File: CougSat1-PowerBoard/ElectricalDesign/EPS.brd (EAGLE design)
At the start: 91.4 x 95.8 mm, 255 parts, among them J1 PV0, J2 PV1, J3 PV2, J4 PV3, J5 Umbilical, J6 SWD, J7 CougSat Card, J8 Deployables, Q1 NTLUD3A50PZ, Q10 DMN2008LFU, Q11 DMN2008LFU, Q12 CSD25402Q3A, Q13 CSD25402Q3A, Q14 NTLUD3A50PZ, Q15 NTLUD3A50PZ, Q16 NTLUD3A50PZ, Q17 NTLUD3A50PZ, Q18 NTLUD3A50PZ, Q19 NTLUD3A50PZ, Q2 NTLUD3A50PZ, Q20 NTLUD3A50PZ, Q21 NTLUD3A50PZ, Q22 NTLUD3A50PZ, Q23 CSD25402Q3A, Q24 CSD25402Q3A, Q25 DMN53D0L, Q26 NTLUD3A50PZ, Q27 NTLUD3A50PZ, Q28 NTLUD3A50PZ, Q29 NTLUD3A50PZ, Q3 NTLUD3A50PZ, Q30 NTLUD3A50PZ, Q31 NTLUD3A50PZ, Q32 NTLUD3A50PZ, Q33 NTLUD3A50PZ, Q34 NTLUD3A50PZ, Q35 NTLUD3A50PZ, Q36 NTLUD3A50PZ, Q37 NTLUD3A50PZ, Q38 NTLUD3A50PZ, Q39 NTLUD3A50PZ, Q4 NTLUD3A50PZ, Q40 NTLUD3A50PZ, Q41 NTLUD3A50PZ, Q42 NTLUD3A50PZ, Q43 NTLUD3A50PZ, Q5 NTLUD3A50PZ, Q6 NTLUD3A50PZ, Q7 NTLUD3A50PZ, Q8 NTLUD3A50PZ, Q9 NTLUD3A50PZ, SW1 D2MQ-1-TL, U1 BQ29700, U10 LTC2499, U11 LTC2499, U12 LTC2499, U13 LTC2499, U14 MCP1501-18, U15 LTC2499, U2 BQ29700, U3 TPS64200, U4 TPS64200, U5 STM32L476RGT, U6 TCA9535R, U7 SN74LVC244AR, U8 TCA9535R, U9 LTC2499

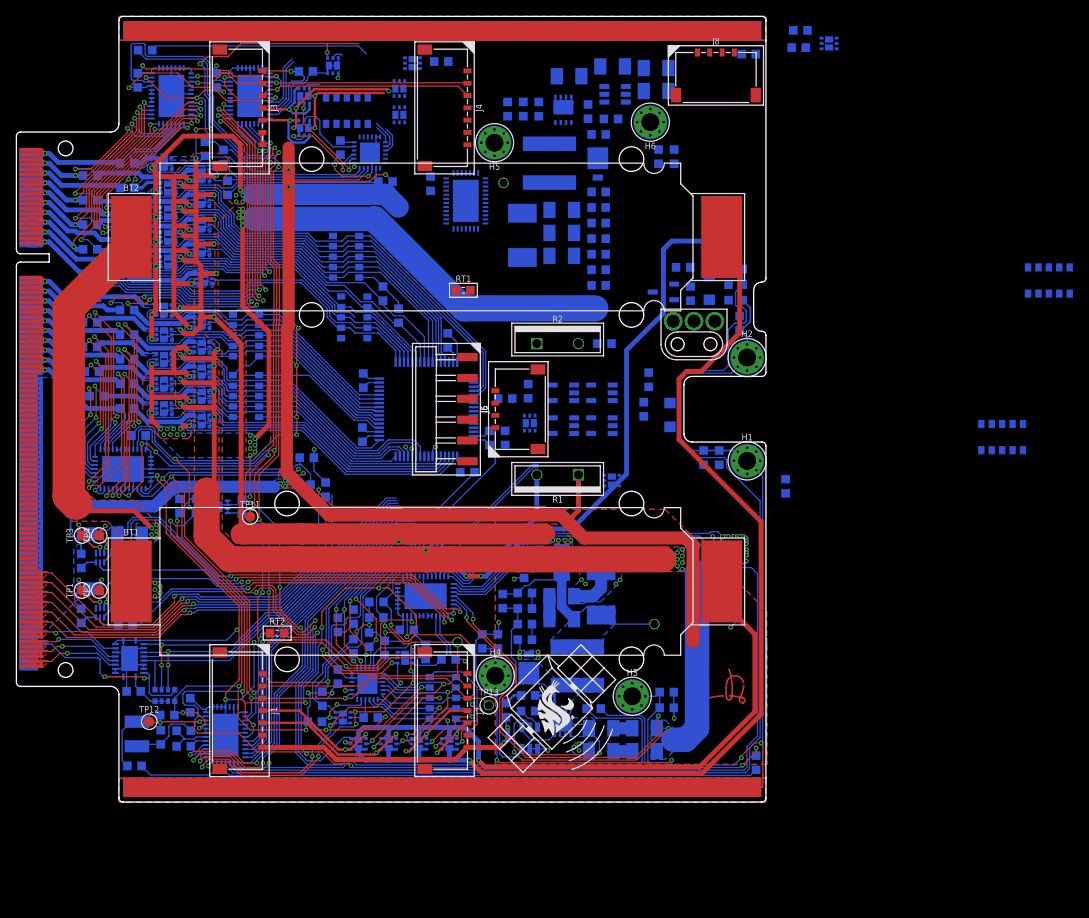
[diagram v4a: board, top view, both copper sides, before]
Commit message: Laid Out JTAG
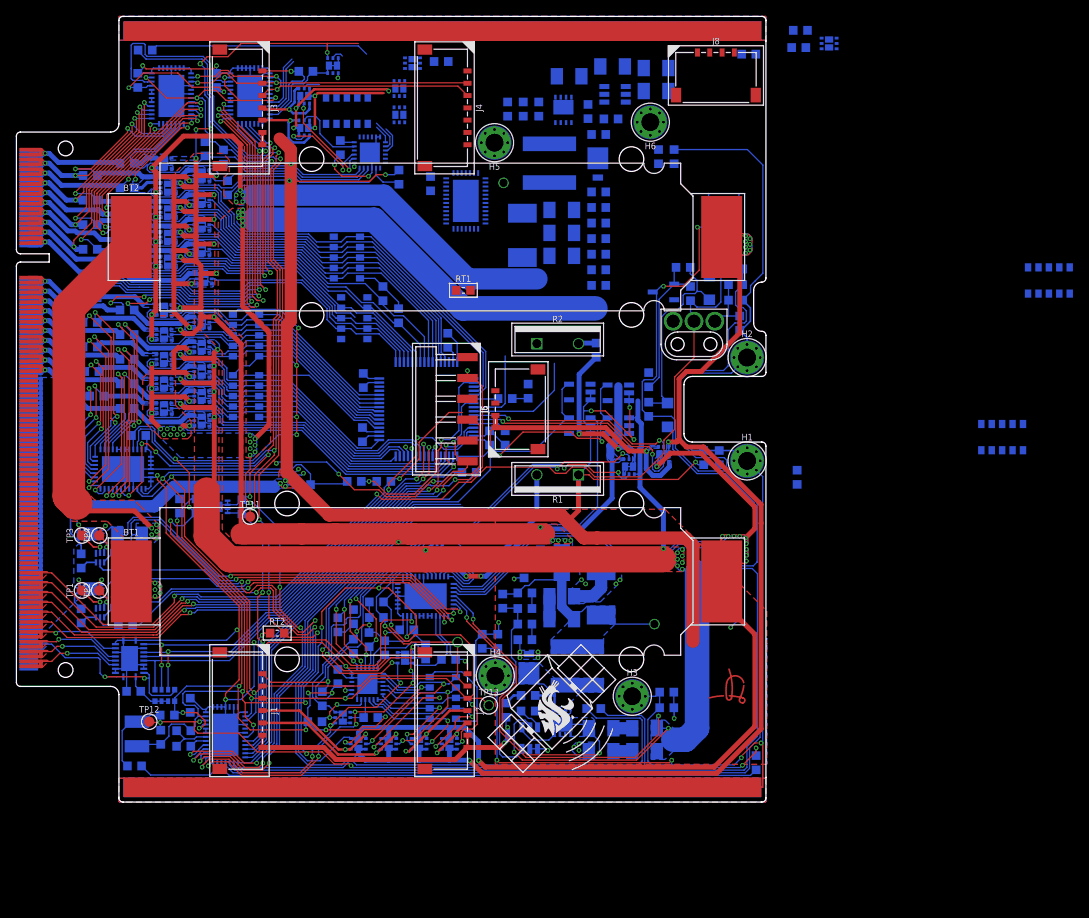
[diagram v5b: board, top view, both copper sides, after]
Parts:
- moved Q9 16.7 mm to (78.9, -5.50), turned to 270 degrees
- moved R78 7.17 mm to (44.8, -8.80), turned to 180 degrees
- moved C22 6.48 mm to (41.2, -8.80)
- moved Q43 2.70 mm to (74.7, -7.00), turned to 90 degrees
- moved D6 2.00 mm to (68.7, 2.10)
- moved D5 2.00 mm to (68.7, -2.00)
- moved D7 2.00 mm to (73.4, -2.00)
- moved D8 2.00 mm to (73.4, 2.00)
- moved R61 1.78 mm to (95.2, -8.30), turned to 270 degrees
- moved R83 1.74 mm to (46.6, 28.3), turned to 270 degrees
- moved R57 1.28 mm to (70.7, 7.20), turned to 270 degrees
- moved R11 0.60 mm to (77.1, 0.00), turned to 270 degrees
- moved D2 0.30 mm to (79.4, -0.70)
- moved RT6 0.20 mm to (55.2, -7.70)
- moved RN2 0.14 mm to (40.3, 18.5)
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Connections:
- net UMB_SW-A: now also U5.58; no longer U5.59
- net UMB_SW-B: now also U5.59; no longer U5.58
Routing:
- net !BATT_SW_CTRL: track 1.19 -> 66.2 mm, vias 1 -> 2
- net PGND: track 382.2 -> 437.4 mm, vias 24 -> 28
- net VIN-A: track 192.7 -> 238.0 mm, vias 14 -> 15
- net PWR_CTRL_SW: track 81.0 -> 122.9 mm
- net CHASSIS: track 224.0 -> 253.1 mm
- net UMB_IN: track 56.0 -> 85.0 mm, vias 1 -> 2
- net VBATT: track 0.00 -> 28.9 mm, vias 0 -> 2
- net UMB_SW-B: track 0.00 -> 27.9 mm, vias 0 -> 2
- net AVDD: track 212.2 -> 239.3 mm, vias 10 -> 13
- net JTAG_TCK: track 43.8 -> 70.3 mm, vias 2 -> 4
- net UMB_SW-A: track 0.00 -> 25.4 mm, vias 0 -> 2
- net BATT_SW_VIN: track 0.00 -> 24.9 mm
- net 3.3V-B: track 159.5 -> 183.8 mm
- net VBATT-A: track 325.1 -> 349.3 mm, vias 19 -> 20
- net I_BH-1: track 0.00 -> 21.8 mm, vias 0 -> 2
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- added copper zone on layer 16, net I_BH-1
- added copper zone on layer 16, net UMB_IN
- added copper zone on layer 1, net VIN-B
- added copper zone on layer 16, net VIN-B

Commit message: Laid Out Regulator B
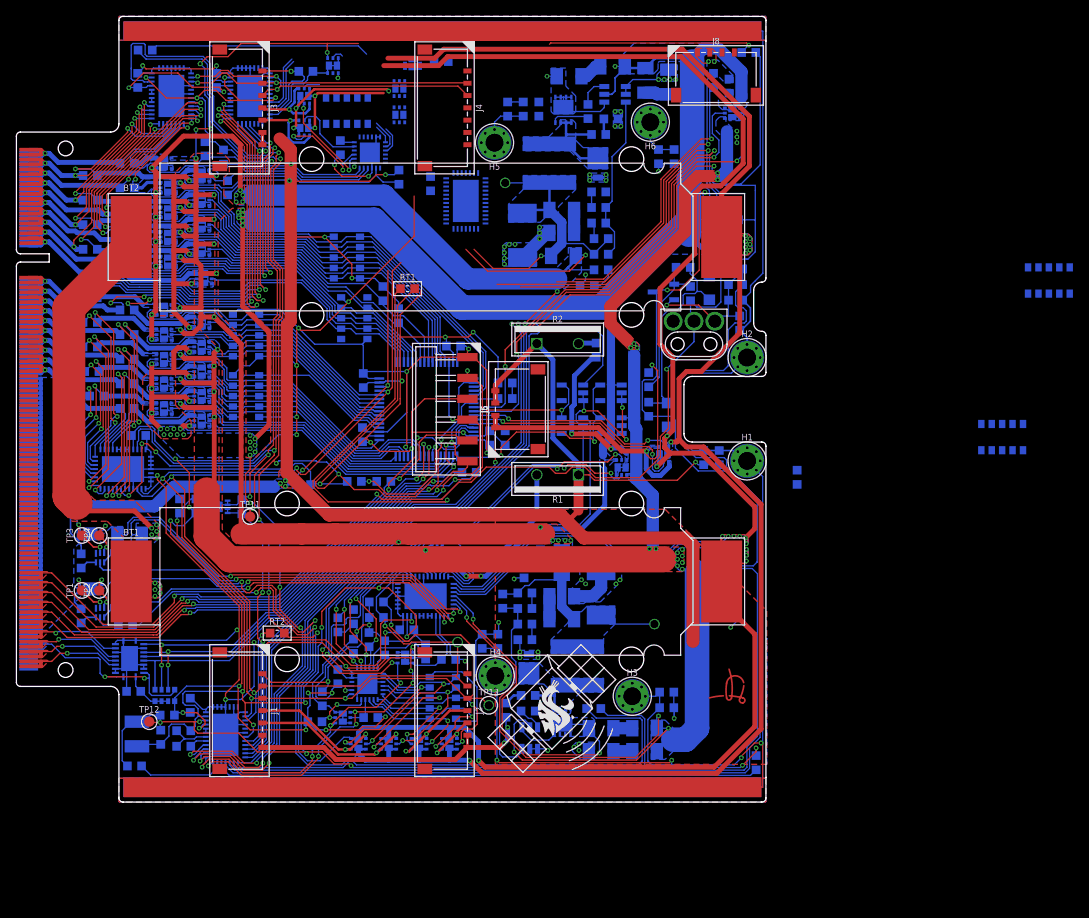
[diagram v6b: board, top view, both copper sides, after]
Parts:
- moved Q41 14.5 mm to (87.3, 36.1), turned to 180 degrees
- moved R55 11.1 mm to (85.0, 40.1), turned to 270 degrees
- moved R70 11.0 mm to (86.9, 39.4), turned to 270 degrees
- moved RT1 6.80 mm to (47.7, 14.7)
- moved R77 2.97 mm to (59.6, 3.20), turned to 180 degrees
- moved C5 1.98 mm to (76.7, 40.1), turned to 270 degrees
- moved C4 1.86 mm to (79.5, 39.9), turned to 90 degrees
- moved R75 1.40 mm to (69.6, 15.1), turned to 180 degrees
- moved DS2 1.00 mm to (85.4, 25.0), turned to 0 degrees
- moved C20 0.99 mm to (53.3, 7.70), turned to 0 degrees
- moved D6 0.91 mm to (67.8, 2.00)
- moved Q43 0.91 mm to (73.8, -7.10)
- moved D5 0.90 mm to (67.8, -2.00)
- moved D7 0.90 mm to (72.5, -2.00)
- moved D8 0.90 mm to (72.5, 2.00)
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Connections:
- net TEMP+X+Y: now also U13.21; no longer U13.12
- net TEMP-BATT-B: now also U13.11; no longer U13.21
- net UMB_IN: now also U13.12; no longer U13.11
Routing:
- net VBATT-B: track 204.3 -> 326.5 mm, vias 35 -> 37
- net VIN-B: track 222.8 -> 330.4 mm, vias 14 -> 15
- net PGND: track 437.4 -> 540.8 mm, vias 28 -> 57
- net TEMP+X+Y: track 45.6 -> 136.8 mm, vias 0 -> 4
- net 3.3V: track 243.0 -> 325.5 mm, vias 20 -> 25
- net 3.3V-B: track 183.8 -> 263.7 mm, vias 25 -> 28
- net DGND: track 254.7 -> 332.9 mm, vias 11 -> 17
- net VIN-A: track 238.0 -> 313.8 mm, vias 15 -> 16
- net AVDD: track 239.3 -> 297.9 mm, vias 13 -> 14
- net CHASSIS: track 253.1 -> 307.3 mm
- net PC_DEPLOY-A: track 9.84 -> 56.1 mm, vias 0 -> 2
- net PC_DEPLOY-B: track 14.2 -> 59.1 mm, vias 0 -> 2
- net VBATT-A: track 349.3 -> 391.7 mm, vias 20 -> 26
- net PR_DEPLOY: track 0.00 -> 37.5 mm, vias 0 -> 3
- net 3.3V_I-B: track 0.00 -> 37.1 mm, vias 0 -> 1
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- added copper zone on layer 16, net 3.3V_I-B
- added copper zone on layer 16, net 3.3V_ISENS-B
- added copper zone on layer 16, net 3.3V_REG_BUCK_NODE-B
- added copper zone on layer 16, net I_DEPLOY
- added copper zone on layer 1, net PR_DEPLOY
- added copper zone on layer 16, net PR_DEPLOY

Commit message: Laid Out Rest of Traces
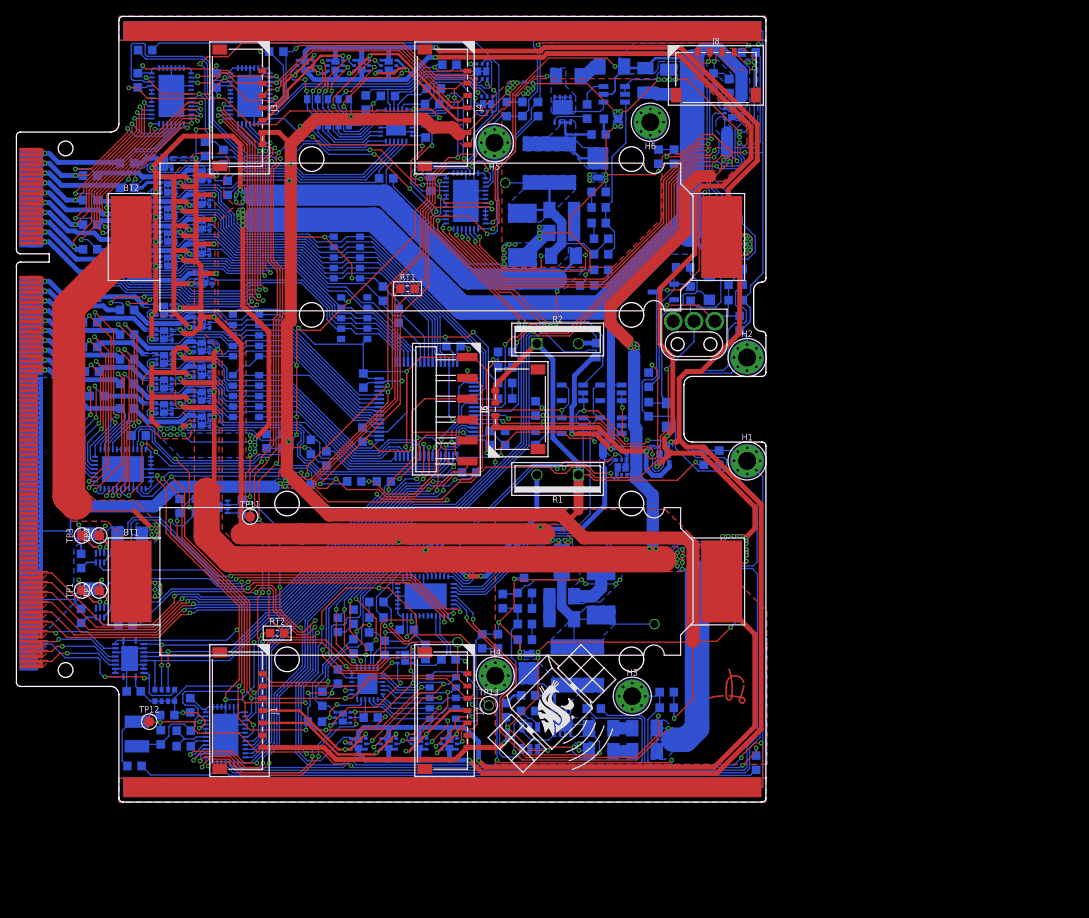
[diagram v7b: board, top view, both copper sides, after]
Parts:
- removed R61: 0Ω <20mΩ, CougsInSpace-Resistors:1608
- removed RN3, RN7: 10kΩ 5%, CougsInSpace-Resistors:3264
- added R100, R101, R102, R103, R104, R105, R94, R95, R96, R97, R98, R99: 10kΩ 0.1%, CougsInSpace-Resistors:1608
- moved Q32 19.4 mm to (57.4, 37.2)
- moved C24 10.6 mm to (49.9, 34.0)
- moved Q33 8.56 mm to (56.8, 41.2), turned to 270 degrees
- moved Q6 8.50 mm to (38.9, 41.9), turned to 180 degrees
- moved Q8 6.14 mm to (45.4, 41.9), turned to 180 degrees
- moved Q7 5.39 mm to (42.1, 41.9), turned to 180 degrees
- moved U6 4.60 mm to (46.3, 34.6), turned to 90 degrees
- moved R46 4.33 mm to (31.7, 43.6)
- moved Q5 3.70 mm to (35.2, 41.9), turned to 180 degrees
- moved RN1 2.31 mm to (38.0, 36.2)
- moved R83 1.56 mm to (45.1, 28.1), turned to 0 degrees
- moved R47 1.08 mm to (52.8, 42.0), turned to 180 degrees
- moved Q12 0.10 mm to (66.6, 36.5)
- moved R15 0.10 mm to (67.3, 40.6)
- moved R16 0.10 mm to (72.6, 41.8)
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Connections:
- net 3.3V: now also R100.2, R101.2, R94.2, R95.2, R96.2, R97.2, R98.2, R99.2
- net 3.3V-B: now also U15.15
- net 3.3V_I-B: now also U15.14
- net 3.3V_ISENS-B: now also U15.13
- net CHASSIS: no longer R61.1
- net DGND: now also U11.12, U11.13, U11.14, U11.15, U15.10, U15.11, U15.22, U15.23, U15.8, U15.9
- net I_BH-1: now also U15.21
- net I_DEPLOY: now also U15.16
- net PC_3.3V-0A: now also U6.4; no longer U6.12
- net PC_3.3V-0B: now also U6.3; no longer U6.11
- net PC_3.3V-1A: now also U6.2; no longer U6.10
- net PC_3.3V-1B: now also U6.1; no longer U6.8
- net PC_BATT-5A: now also R102.2
- net PC_BATT-5B: now also R103.2
- net PC_BATT-6A: now also R104.2
- net PC_BATT-6B: now also R105.2
- net PC_DEPLOY-A: now also R98.1
- net PC_DEPLOY-B: now also R99.1
- net PGND: now also R102.1, R103.1, R104.1, R105.1; no longer R61.2, RN3.10, RN3.5, RN7.10, RN7.5
- net PR_BH-1: now also U15.20
- net PR_DEPLOY: now also U15.17
- net PVC_3.3V-2A: now also R94.1, U6.16; no longer U6.3
- net PVC_3.3V-2B: now also R95.1, U6.17; no longer U6.2
- net PVC_3.3V-3A: now also R96.1, U6.15
- net PVC_3.3V-3B: now also R97.1, U6.14
- net PVI_3.3V-2: now also U11.9; no longer U11.11
- net PVI_3.3V-3: now also U11.11; no longer U11.9
- net PV_3.3V-2: now also U11.8; no longer U11.10
- net PV_3.3V-3: now also U11.10; no longer U11.8
- net PV_SW-4A: now also RN1.6, U6.5; no longer RN1.1, U6.13, U6.14
- net PV_SW-4B: now also RN1.4, U6.6; no longer RN1.2, U6.1
- net PV_SW-5A: now also RN1.7, U6.7; no longer RN1.3, U6.15
- net PV_SW-5B: now also RN1.8, U6.10; no longer RN1.4, U6.17
- net PV_SW-6A: now also RN1.3, U6.8; no longer RN1.6
- net PV_SW-6B: now also RN1.9, U6.12; no longer RN1.7
- net PV_SW-7A: now also RN1.2, U6.11; no longer RN1.8
- net PV_SW-7B: now also RN1.1, U6.13; no longer RN1.9
- net UMB_SW-A: now also R100.1
- net UMB_SW-B: now also R101.1
- net VBATT-B: now also U15.12, U15.18
- net VIN-B: now also U15.19
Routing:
- net PGND: track 540.8 -> 779.0 mm, vias 57 -> 73
- net CHASSIS: track 307.3 -> 441.8 mm, vias 4 -> 7
- net 3.3V: track 325.5 -> 401.9 mm, vias 25 -> 32
- net DGND: track 332.9 -> 403.3 mm, vias 17 -> 19
- net VBATT-B: track 326.5 -> 395.7 mm, vias 37 -> 39
- net TEMP-X+Y: track 99.0 -> 161.1 mm, vias 1 -> 2
- net I2C_SDA: track 175.6 -> 221.6 mm, vias 8 -> 11
- net I2C_SCL: track 187.9 -> 231.4 mm, vias 9 -> 12
- net TEMP-REG-B: track 81.9 -> 124.1 mm, vias 3 -> 4
- net AVDD: track 297.9 -> 337.8 mm, vias 14 -> 16
- net 3.3V-B: track 263.7 -> 301.0 mm, vias 28 -> 30
- net 3.3V-A: track 256.4 -> 292.3 mm, vias 31 -> 32
- net AGND: track 225.0 -> 257.1 mm, vias 17 -> 22
- net I_BH-1: track 21.5 -> 52.1 mm, vias 2 -> 4
- net VBATT-A: track 391.7 -> 419.5 mm
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
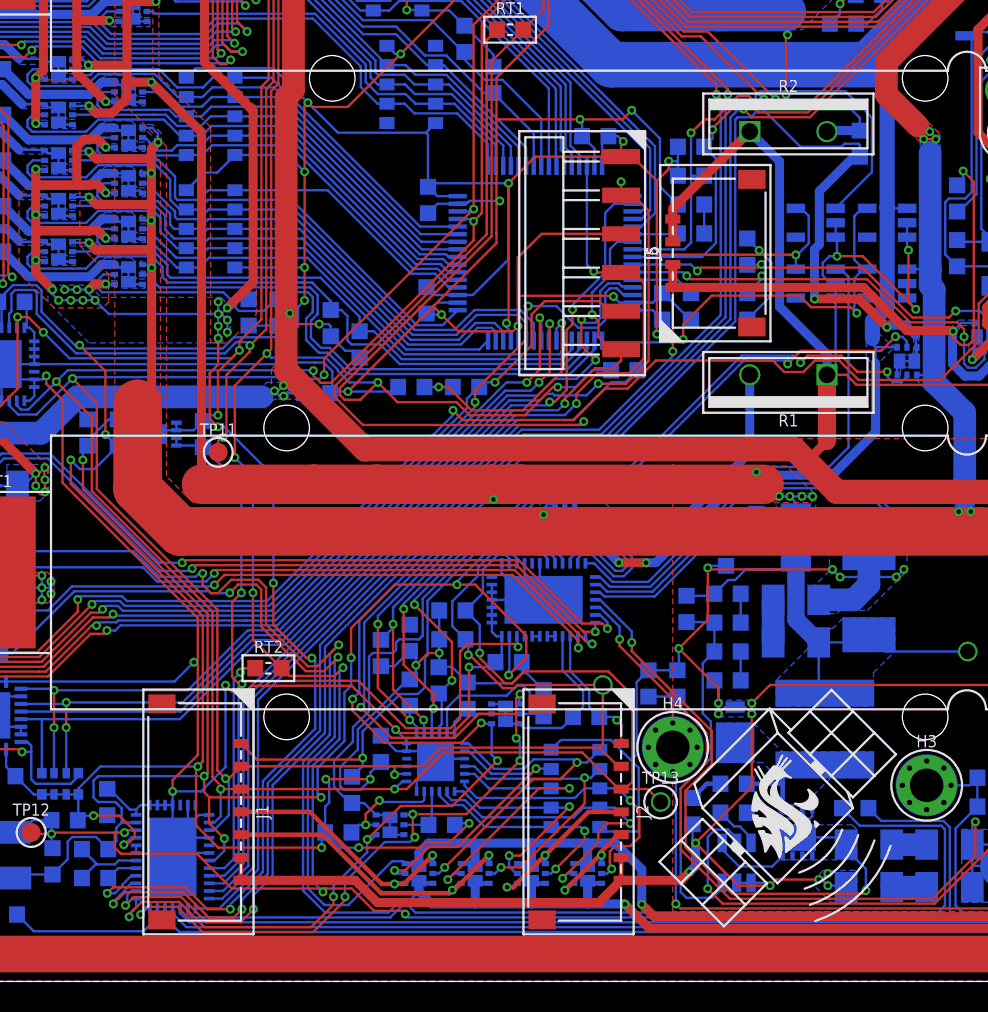
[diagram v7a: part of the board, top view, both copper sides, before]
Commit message: Fixed Off Schematic Layout
Fitting onto one page and off sheet connectors
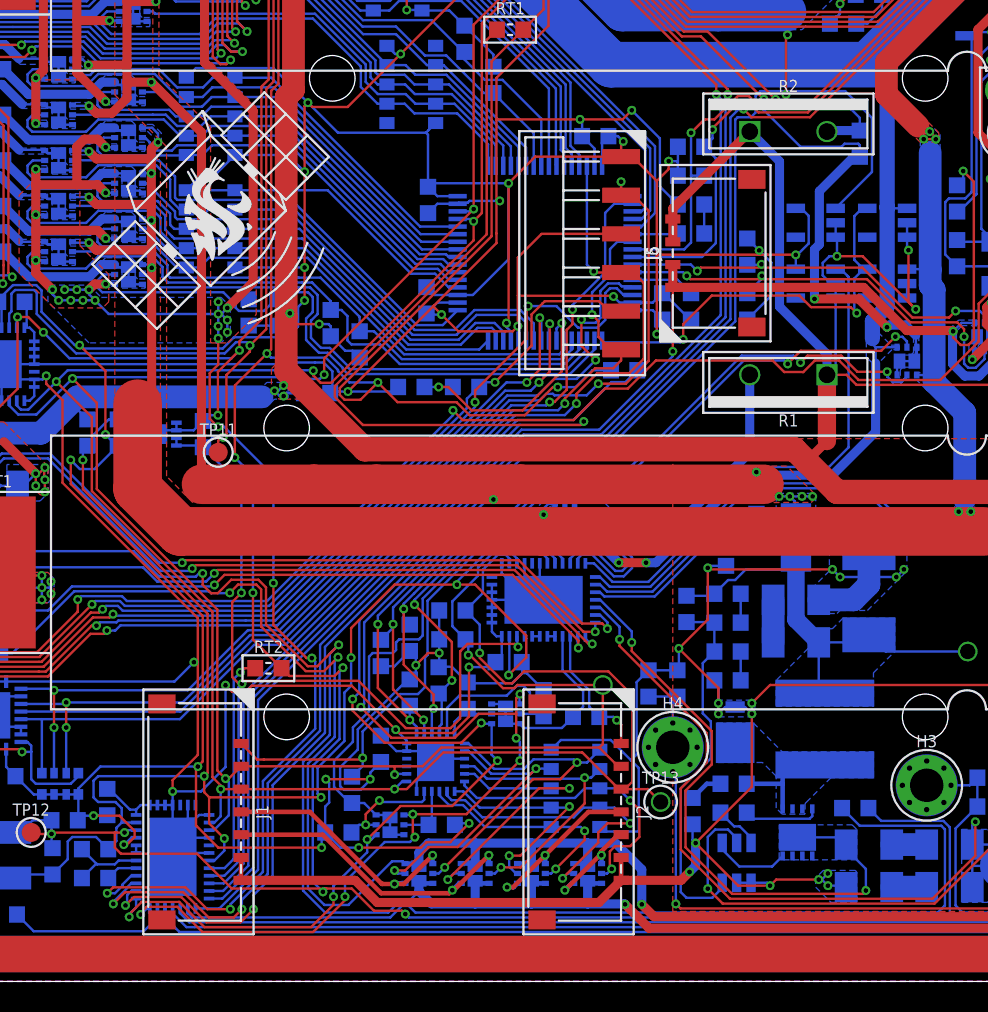
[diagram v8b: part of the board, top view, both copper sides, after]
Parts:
- moved LOGO1 54.2 mm to (28.0, 2.80)
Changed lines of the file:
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@@
 <wire x1="33.7" y1="27.5" x2="34.5" y2="27.5" width="0.15" layer="22" locked="yes"/>
 <wire x1="34.5" y1="27.5" x2="34.5" y2="12" width="0.15" layer="22" locked="yes"/>
-<wire x1="0" y1="0" x2="93.4" y2="0" width="0.2" layer="49"/>
 </plain>
 <attributes>
@@
 <attribute name="TEMP" value="70°C Max 2A" x="44.8" y="-8.8" size="0.8" layer="28" font="vector" ratio="15" rot="MR180" display="off"/>
 </element>
-<element name="LOGO1" library="CougsInSpace-Aesthetics" package="CIS-SATELLITE-16" value="Satellite 16mm" x="65.3" y="-36.5" rot="R90"/>
+<element name="LOGO1" library="CougsInSpace-Aesthetics" package="CIS-SATELLITE-16" value="Satellite 16mm" x="28" y="2.8" rot="R90"/>
 <element name="LOGO2" library="CougsInSpace-Aesthetics" package="SIGN-BRADLEY" value="SIGNATUREBRADLEY" x="86.7" y="-33.7" rot="R90"/>
 <element name="R79" library="CougsInSpace-Resistors" package="1608" value="0Ω &lt;20mΩ" x="62.4" y="-36.8" rot="MR180">
